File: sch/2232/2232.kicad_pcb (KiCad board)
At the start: 2 copper layers, 80 x 70 mm, 74 parts, among them J1 47346-0001, J2 IDC-06, J3 IDC-06, J4 IDC-10, J5 IDC-10, J6 6P6C, J7 Screw_Terminal_01x06, J8 Screw_Terminal_01x06, Q1 BC817-40, Q2 FZT1049A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

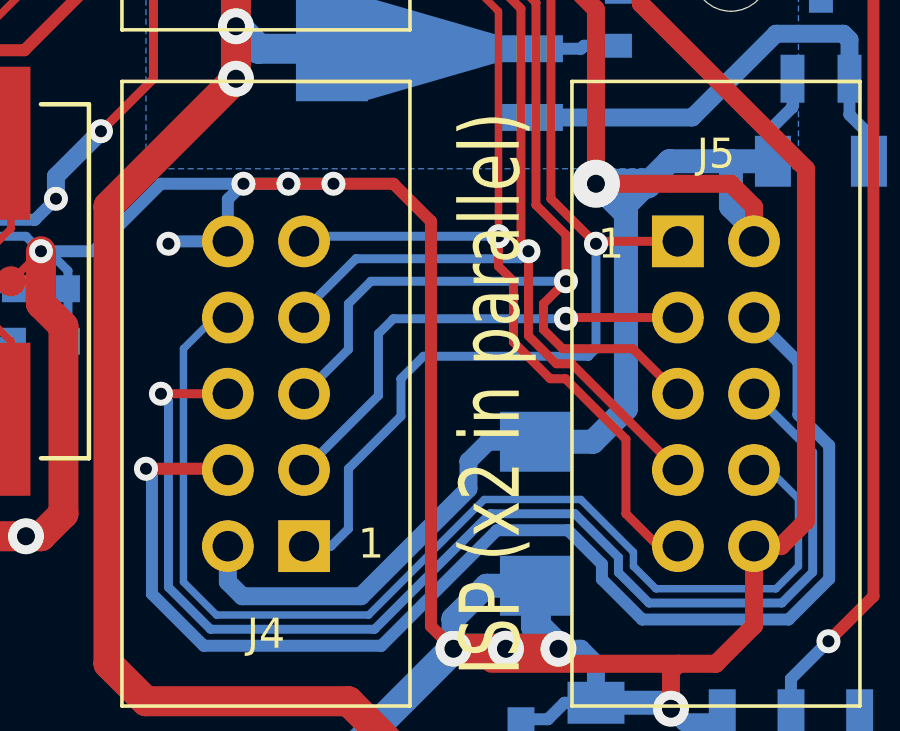
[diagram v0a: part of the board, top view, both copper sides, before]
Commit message: Pullups to RST and MISO added
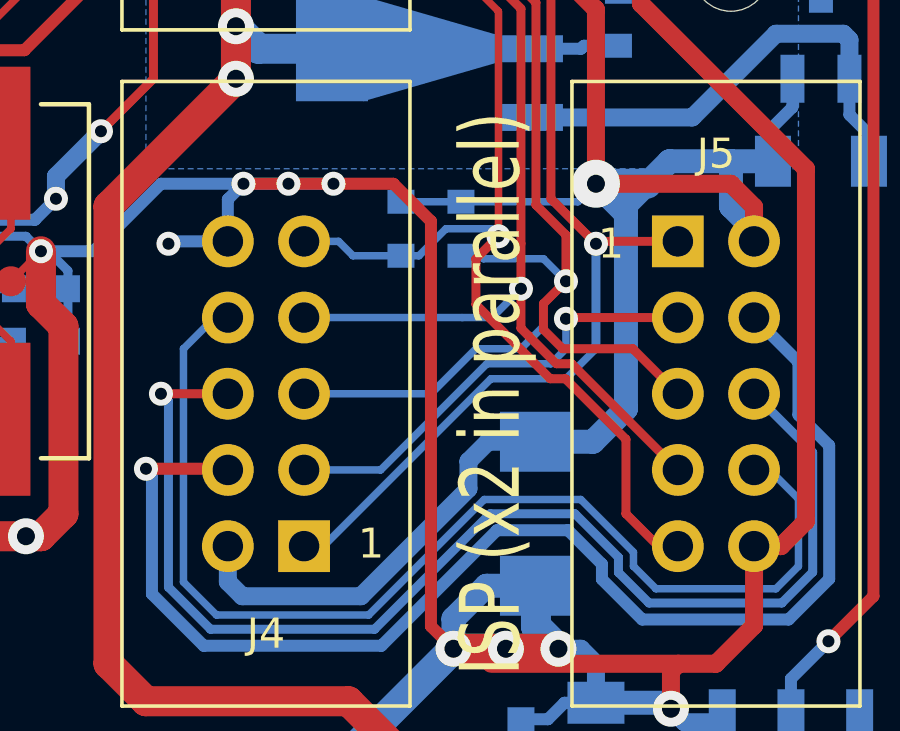
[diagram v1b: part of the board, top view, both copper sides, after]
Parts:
- added R14: 10k, NevaDA:R_0603, B.Cu at (124.0, 99.5)
- added R15: 10k, NevaDA:R_0603, B.Cu at (122.0, 99.5)
- R11, R12, R13, R8: value 100 -> 110
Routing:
- net /IDC_VCC: track 65.5 -> 72.3 mm
- net /IDC_RST: track 49.4 -> 52.8 mm
- net /IDC_MOSI: track 52.7 -> 50.8 mm
- net /IDC_MISO: track 52.2 -> 53.4 mm
- net /IDC_CLK: track 49.7 -> 48.8 mm
- net /IDC_R: track 15.8 -> 15.1 mm

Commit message: Silk updates
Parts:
- moved R15 3.25 mm to (125.2, 99.5)
- moved R14 2.75 mm to (126.8, 99.5)
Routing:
- net /IDC_VCC: track 72.3 -> 69.0 mm
- net GNDD: track 1047.2 -> 1044.2 mm, vias 84 -> 82
- net /IDC_RST: track 52.8 -> 50.4 mm
- net /IDC_MISO: track 53.4 -> 54.4 mm
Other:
- board text added: "6pin"
- board text added: "micro"
- board text removed: "WPROG version 1.0"

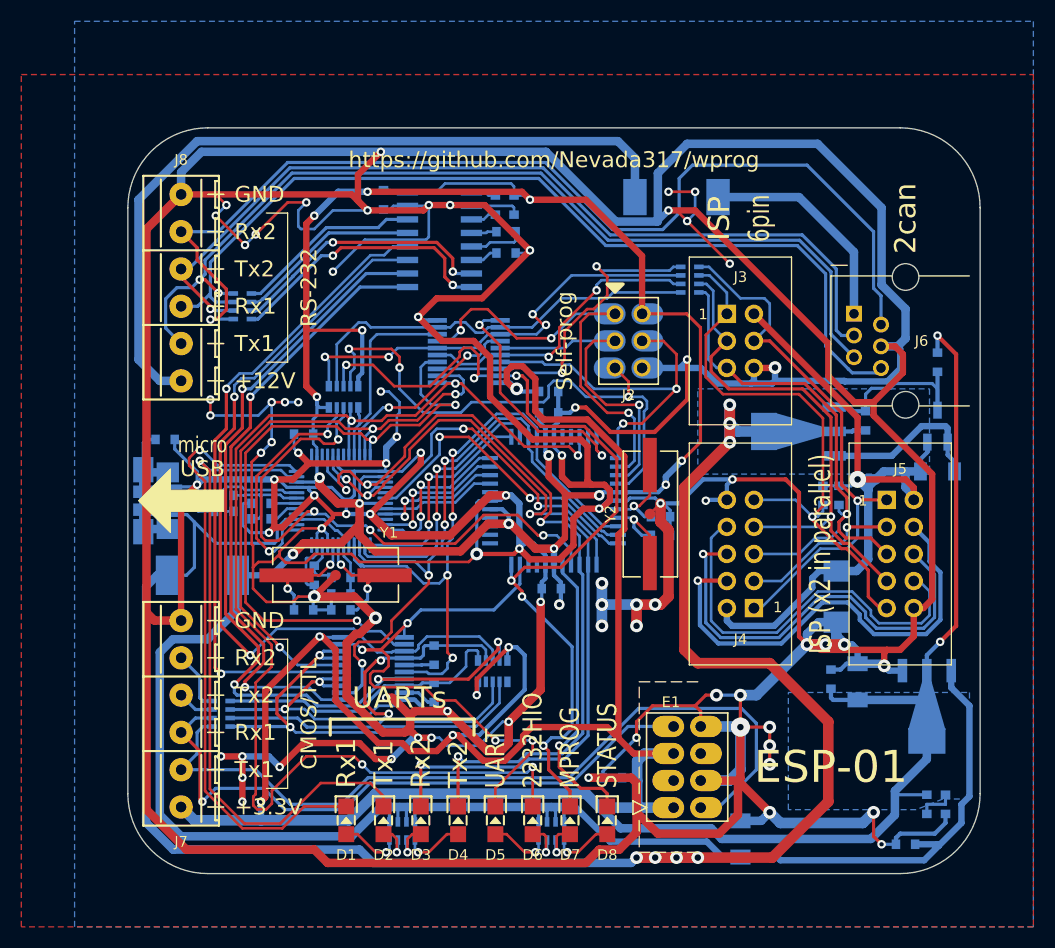
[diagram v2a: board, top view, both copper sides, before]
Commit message: Reset button added
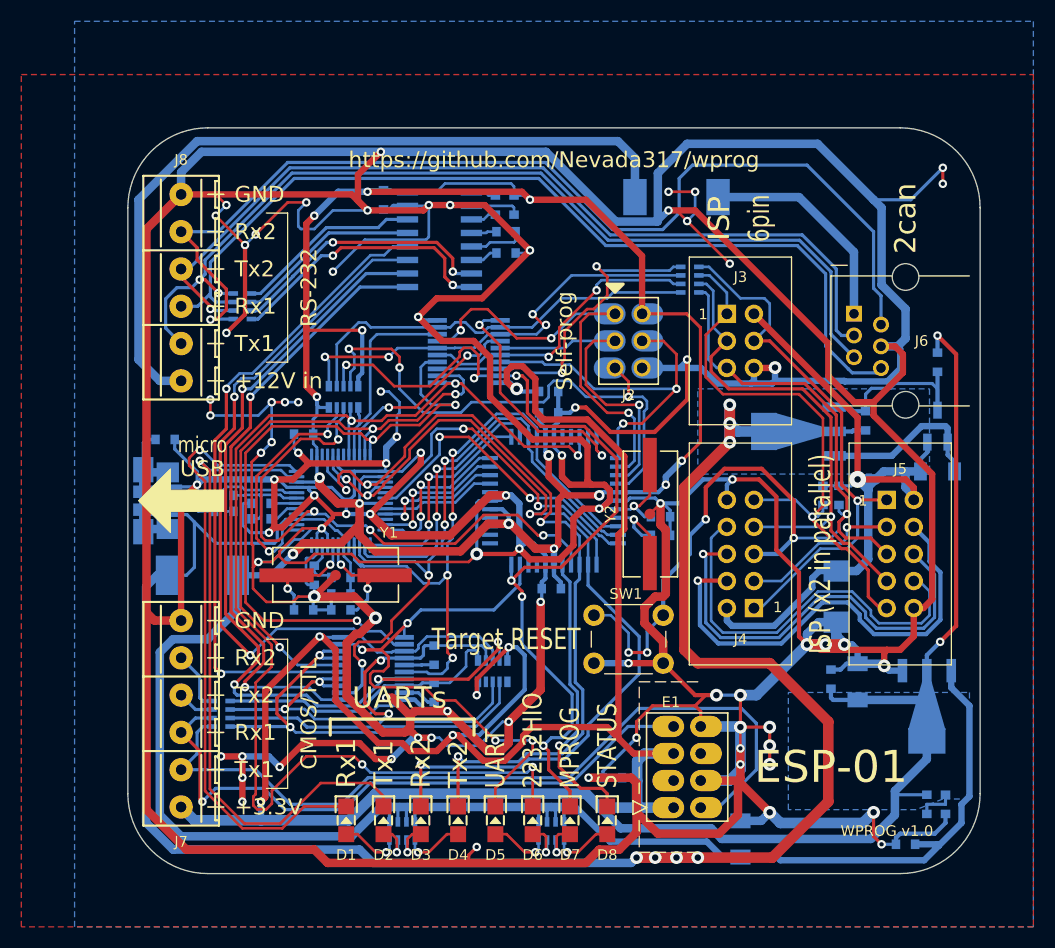
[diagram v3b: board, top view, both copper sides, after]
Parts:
- added SW1: Button 6mm, NevaDA:SW_PUSH_6mm, F.Cu at (110.2, 115.2)
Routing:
- net /IDC_RST: track 50.4 -> 89.4 mm, vias 1 -> 5
- net GNDD: track 1044.2 -> 1077.8 mm, vias 82 -> 83
- net /LED3_~RD: track 79.5 -> 83.4 mm
- net +5V: track 339.4 -> 337.9 mm, vias 15 -> 14
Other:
- board text added: "+12V in"
- board text added: "Target RESET"
- board text added: "WPROG v1.0"
- board text removed: "+12V"
